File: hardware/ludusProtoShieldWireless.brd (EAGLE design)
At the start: 59.7 x 53.3 mm, 72 parts, among them Q1 MOSFET-NCHANNELSMD, Q2 MOSFET-NCHANNELSMD, U1 ARDUINO, U3 TB6612FNG

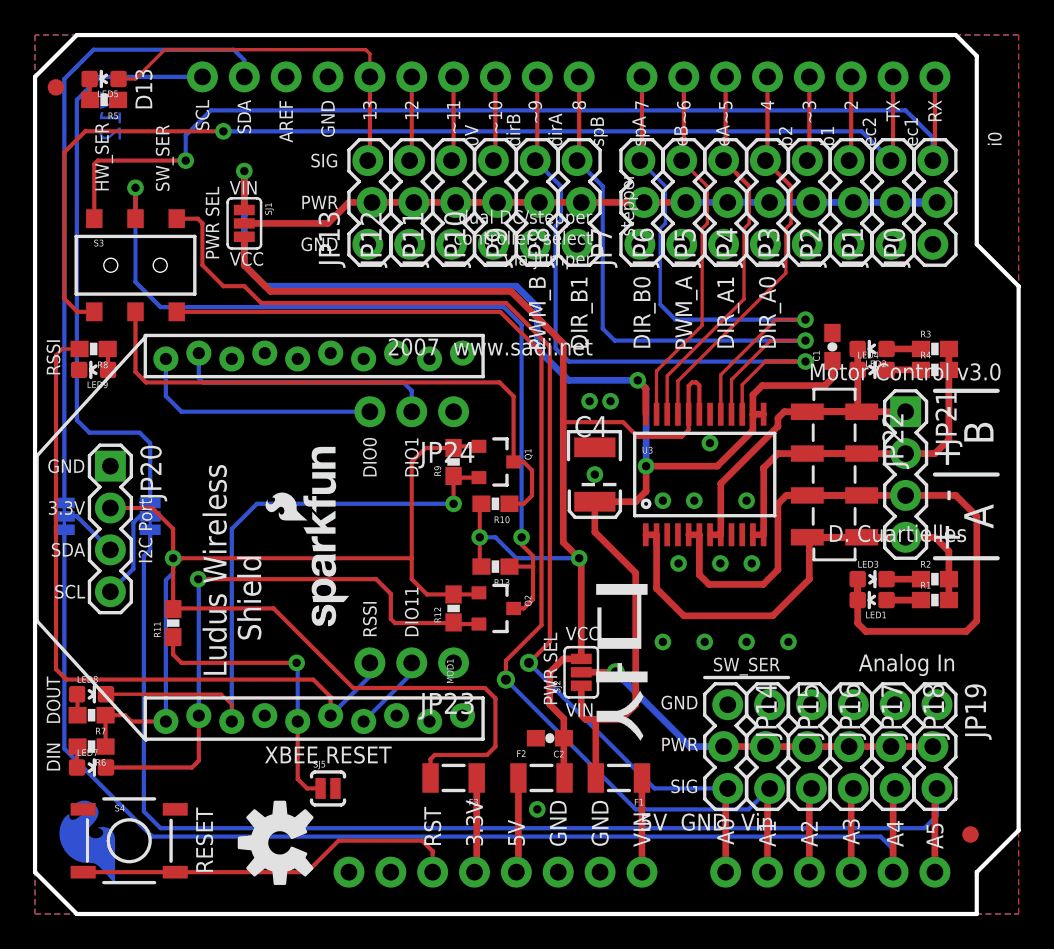
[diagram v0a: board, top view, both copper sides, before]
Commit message: Updated shield footprint to include staggered / locking holes
* changed filenames to ludusProtoShieldWireless
* repo name will change after this commit
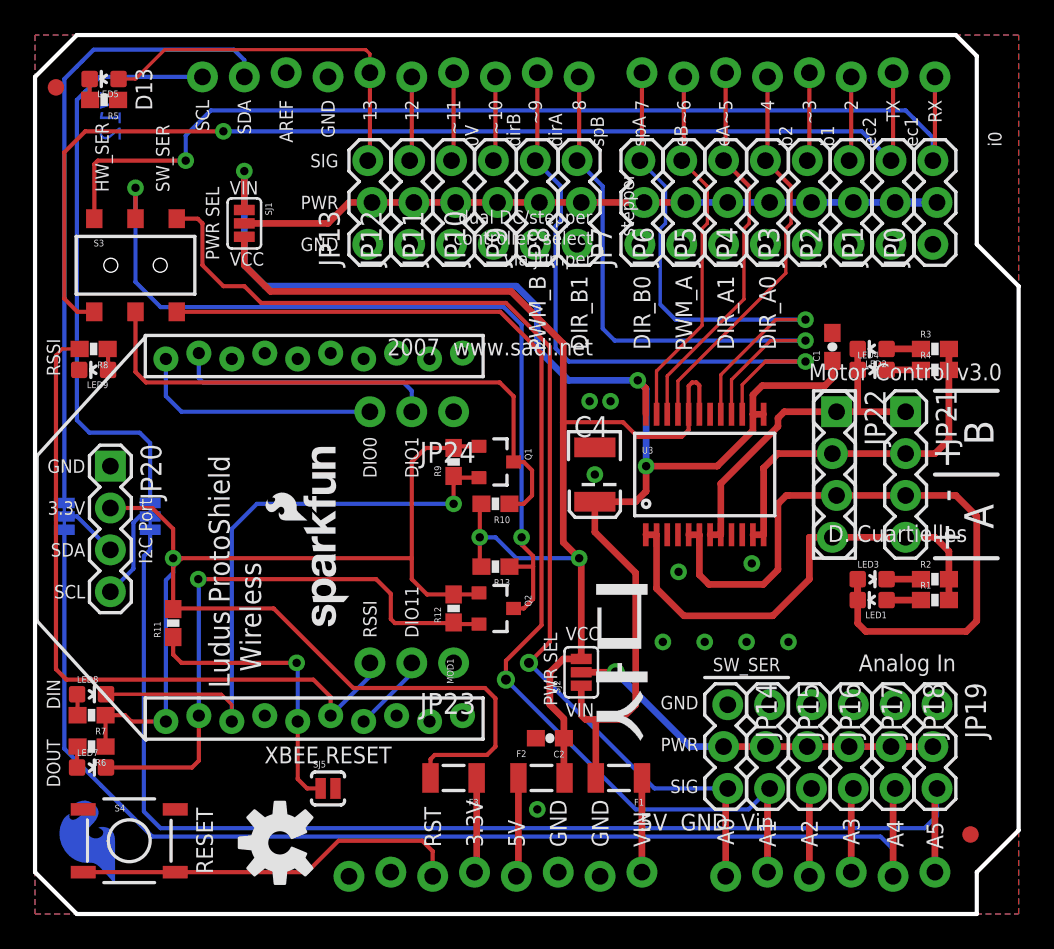
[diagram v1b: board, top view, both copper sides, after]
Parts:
- JP22: device SparkFun-Connectors:1X04_SMD_STRAIGHT_COMBO -> SparkFun-Connectors:1X04_LOCK
- U1: device SparkFun-Boards:UNO_R3_SHIELD_NOLABELS -> SparkFun-Boards:UNO_R3_SHIELD_NOLABELS_LOCK
- moved U$1 2.54 mm to (42.7, 26.9)
- moved LOGO4 0.77 mm to (19.4, 28.3)
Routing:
- net A4: track 72.6 -> 73.1 mm
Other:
- board text added: "Ludus ProtoShield Wireless"
- board text removed: "Ludus Wireless Shield"

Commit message: Updated to fix all issues -
Also added a switch to shield for switching between VIN and 5V
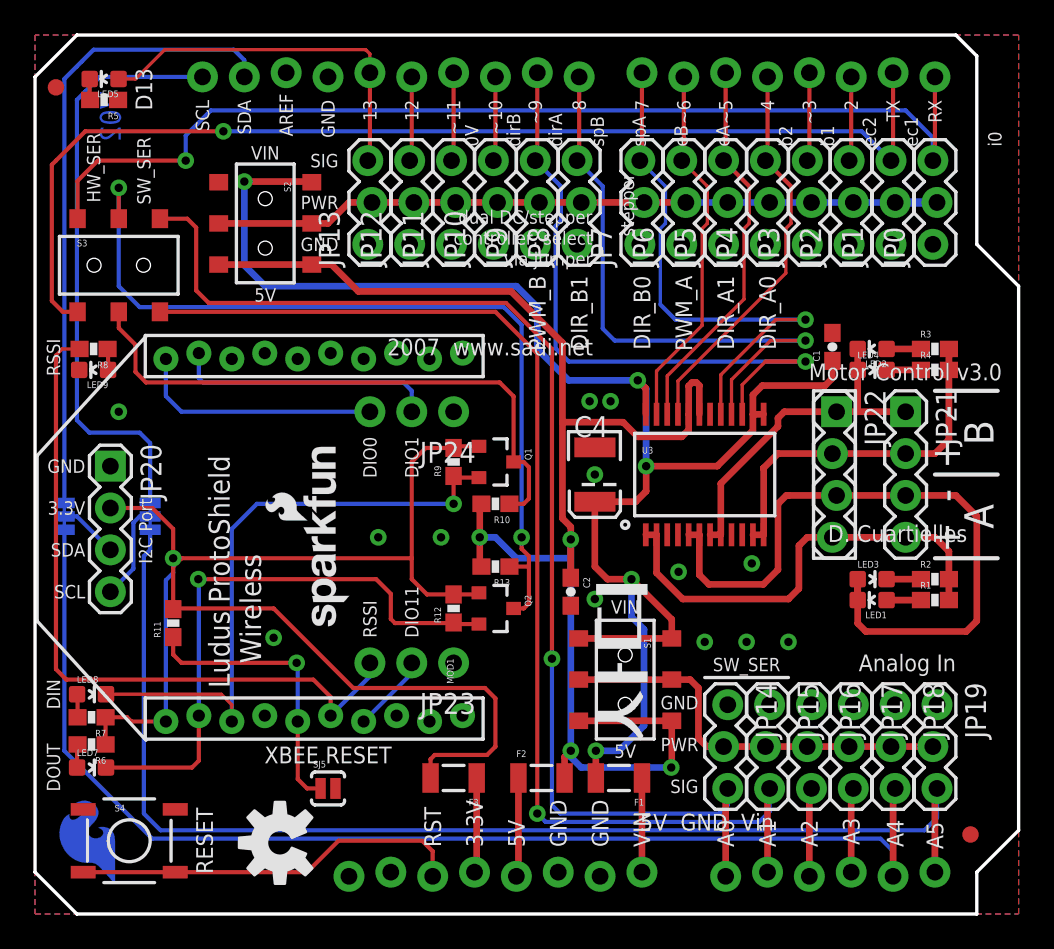
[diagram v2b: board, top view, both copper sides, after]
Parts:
- removed SJ1, SJ2: JUMPER-PAD-3-2OF3_NC_BY_PASTE, SparkFun-Passives:PAD-JUMPER-3-2OF3_NC_BY_PASTE_YES_SILK_FULL_BOX
- added S1, S2: (no value), SparkFun-Electromechanical:AYZ0202
- Q1, Q2: value MOSFET-NCHANNELSMD -> MOSFET-NCHANNELBSS138
- U$1: value SFE_LUDUS -> SFE_LUDUSSFE_LUDUS-M
- moved C2 8.98 mm to (32.5, 19.6), turned to 270 degrees
- moved S3 1.02 mm to (5.08, 39.4)
- moved U$1 0.92 mm to (41.8, 27.2), flipped to the bottom, turned to 270 degrees
- moved R6 0.13 mm to (3.43, 10.3)
- moved R7 0.13 mm to (3.43, 11.9)
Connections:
- net ANALOG_PWR_RAIL: now also S1.2; no longer SJ2.2
- net FUSED_5V: now also S1.3, S2.3; no longer SJ1.3, SJ2.3
- net FUSED_VIN: now also S1.1, S2.1; no longer SJ1.1, SJ2.1
- net PWR_RAIL: now also S2.2; no longer SJ1.2
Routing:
- net A0/SW_RXI: track 67.7 -> 74.5 mm
- net N$6: track 0.00 -> 5.59 mm
- net N$11: track 0.00 -> 5.59 mm
- net N$2: track 0.00 -> 5.46 mm
- net N$4: track 0.00 -> 5.33 mm
- net N$10: track 0.00 -> 5.33 mm
- net A1/SW_TXO: track 68.8 -> 73.0 mm
- net FUSED_VIN: track 87.9 -> 92.0 mm, vias 3 -> 5
- net PWR_RAIL: track 42.6 -> 38.5 mm
- net ANALOG_PWR_RAIL: track 23.2 -> 19.3 mm, vias 1 -> 0
- net FUSED_5V: track 75.5 -> 79.3 mm, vias 2 -> 4
- net AOUT1: track 29.4 -> 28.1 mm
- net XBEE_RXI: track 51.9 -> 52.6 mm
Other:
- board text added: "V02"
- board text removed: "PWR SEL"
- board text removed: "V12"
- board text removed: "VCC"
